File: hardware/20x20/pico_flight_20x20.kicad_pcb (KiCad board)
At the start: 2 copper layers, 28 x 28 mm, 39 parts, among them J1 USB_B_Micro, J4 ESC_AIKON32, U1 MCP1711T-33I_OT, U2 W25Q128JVS, U3 RP2040, U4 MPU-9250, Y1 SMD-3225_4P__12MHZ_20PF_10PPM

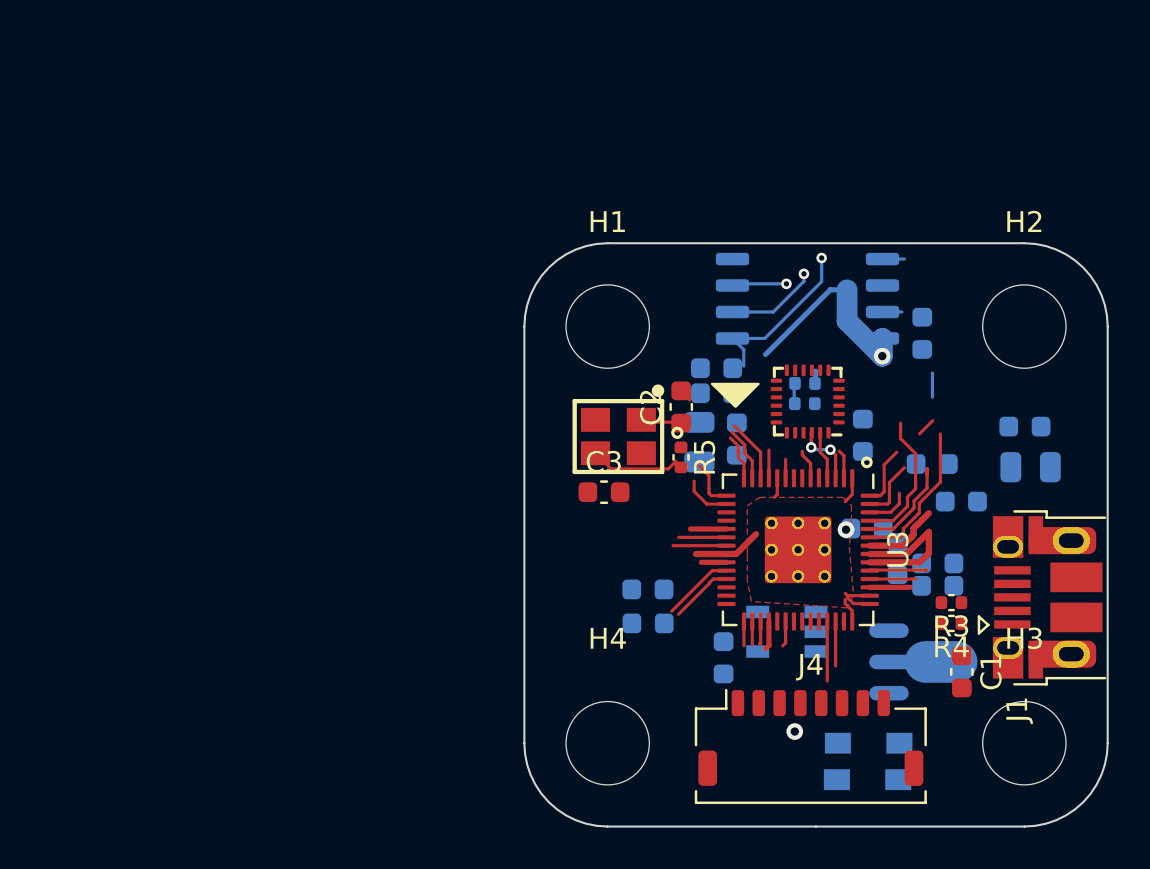
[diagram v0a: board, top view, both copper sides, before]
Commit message: Add implot, test mahi-gui, progress on pcb
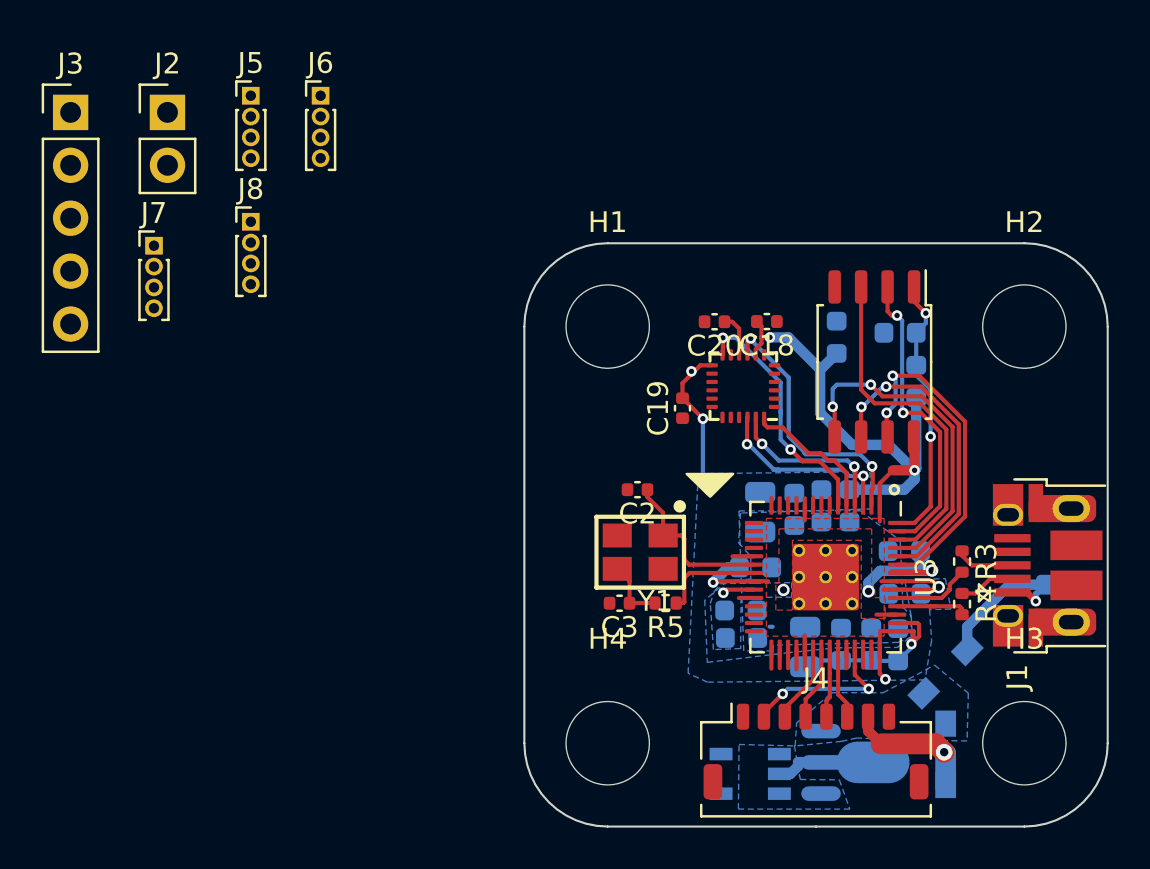
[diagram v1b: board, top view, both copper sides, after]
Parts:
- added J2: Conn_01x02, Connector_PinHeader_2.54mm:PinHeader_1x02_P2.54mm_Vertical, F.Cu at (-21.1, -10.3)
- added J3: DEBUG, Connector_PinHeader_2.54mm:PinHeader_1x05_P2.54mm_Vertical, F.Cu at (-25.8, -10.3)
- added J5: UART1, Connector_PinHeader_1.00mm:PinHeader_1x04_P1.00mm_Vertical, F.Cu at (-17.1, -11.1)
- added J6: UART2, Connector_PinHeader_1.00mm:PinHeader_1x04_P1.00mm_Vertical, F.Cu at (-13.8, -11.1)
- added J7: CAM, Connector_PinHeader_1.00mm:PinHeader_1x04_P1.00mm_Vertical, F.Cu at (-21.8, -3.88)
- added J8: VTX, Connector_PinHeader_1.00mm:PinHeader_1x04_P1.00mm_Vertical, F.Cu at (-17.1, -5.03)
- C1: moved to B.Cu
- C18, C19, C20: footprint Capacitor_SMD:C_0603_1608Metric -> Capacitor_SMD:C_0402_1005Metric; moved to F.Cu
- C2, C3: footprint Capacitor_SMD:C_0603_1608Metric -> Capacitor_SMD:C_0402_1005Metric
- R1, R2: footprint Capacitor_SMD:C_0402_1005Metric -> Capacitor_SMD:C_0603_1608Metric
- R3, R4, R5: footprint Capacitor_SMD:C_0402_1005Metric -> Resistor_SMD:R_0402_1005Metric
- U2: moved to F.Cu
- moved C4 13.8 mm to (9.48, 15.4), turned to 90 degrees
- moved C11 12.8 mm to (12.7, 15.2), turned to 90 degrees
- moved C7 12.4 mm to (6.42, 14.9)
- moved C19 8.86 mm to (3.59, 3.92), turned to 90 degrees
- moved U1 7.04 mm to (6.84, 21.5)
- moved R5 7.03 mm to (2.78, 13.3), turned to 180 degrees
- moved C13 6.83 mm to (7.09, 11.6), turned to 0 degrees
- moved C9 6.37 mm to (14.3, 12.8), turned to 180 degrees
- moved C1 6.36 mm to (21.8, 12.4), turned to 0 degrees
- moved C16 6.29 mm to (11.6, 8.61), turned to 270 degrees
- moved VR2 5.82 mm to (10.2, 20.9)
- moved R1 5.70 mm to (14.0, 0.30), turned to 180 degrees
- moved C15 5.68 mm to (11.2, 15.2)
- moved Y1 5.65 mm to (1.56, 10.8)
- moved C3 5.38 mm to (0.57, 13.3), turned to 180 degrees
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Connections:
- net VIDEO_IN renamed Net-(U3-Pad41)
- net VIDEO_OUT_SIG renamed Net-(U3-Pad18)
- net VIDEO_OUT_SYNC renamed Net-(U3-Pad17)
- U3 pad 34: Net-(U3-Pad34) -> ESC_MOTOR_4
- U3 pad 35: Net-(U3-Pad35) -> ESC_MOTOR_3
- U3 pad 36: Net-(U3-Pad36) -> ESC_MOTOR_2
- U3 pad 37: Net-(U3-Pad37) -> ESC_MOTOR_1
- U3 pad 39: Net-(U3-Pad39) -> ESC_CURRENT
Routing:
- net +3V3: track 28.4 -> 58.9 mm, vias 2 -> 8
- net /QSPI_SD2: track 4.72 -> 16.6 mm, vias 1 -> 0
- net IMU_DATA_RDY: track 1.47 -> 13.0 mm, vias 0 -> 2
- net IMU_SPI_MISO: track 1.39 -> 12.9 mm, vias 0 -> 2
- net /QSPI_SCLK: track 5.01 -> 15.1 mm, vias 0 -> 2
- net /QSPI_SD0: track 7.60 -> 16.6 mm, vias 0 -> 2
- net Net-(C1-Pad1): track 0.00 -> 7.99 mm, vias 0 -> 1
- net ESC_CURRENT: track 0.00 -> 7.90 mm, vias 0 -> 2
- net /QSPI_SD1: track 7.34 -> 14.8 mm, vias 1 -> 2
- net /QSPI_SD3: track 9.07 -> 16.3 mm, vias 0 -> 2
- net IMU_SPI_MOSI: track 0.42 -> 6.81 mm
- net VBAT: track 0.00 -> 6.37 mm, vias 0 -> 1
- net IMU_SPI_CS: track 3.15 -> 9.26 mm
- net IMU_SPI_SCLK: track 2.32 -> 8.13 mm, vias 0 -> 2
- net +1V1: track 6.83 -> 11.1 mm, vias 0 -> 4
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- added copper zone on B.Cu, net +1V1
- added copper zone on F.Cu, net +1V1
- added copper zone on B.Cu, net +3V3
- added copper zone on B.Cu, net +5V
- added copper zone on B.Cu, net GND
- added copper zone on B.Cu, net VBUS

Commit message: 45 degree layout
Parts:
- moved C3 6.21 mm to (4.58, 18.0), turned to 225 degrees
- moved C2 5.73 mm to (1.34, 13.6), turned to 225 degrees
- moved Y1 5.15 mm to (3.55, 15.6), turned to 225 degrees
- moved R4 4.69 mm to (16.2, 8.70), turned to 225 degrees
- moved R5 4.62 mm to (6.14, 16.4), turned to 225 degrees
- moved C1 4.10 mm to (21.9, 8.29)
- moved J1 4.10 mm to (22.4, 7.36)
- moved C10 4.04 mm to (14.9, 11.3), turned to 135 degrees
- moved C18 3.76 mm to (5.24, 2.66)
- moved C19 3.76 mm to (1.19, 6.82)
- moved C20 3.76 mm to (2.73, 2.67)
- moved U4 3.76 mm to (4.11, 5.76)
- moved C8 3.68 mm to (11.9, 7.95), turned to 225 degrees
- moved C9 3.56 mm to (13.4, 9.38), turned to 225 degrees
- moved R3 3.55 mm to (15.6, 8.04), turned to 225 degrees
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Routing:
- net +3V3: track 58.9 -> 29.1 mm, vias 8 -> 5
- net /QSPI_SD2: track 16.6 -> 0.00 mm
- net /QSPI_SD0: track 16.6 -> 1.49 mm, vias 2 -> 1
- net /QSPI_SD3: track 16.3 -> 2.01 mm
- net /QSPI_SCLK: track 15.1 -> 1.59 mm
- net IMU_SPI_MISO: track 12.9 -> 1.76 mm, vias 2 -> 1
- net IMU_DATA_RDY: track 13.0 -> 2.12 mm, vias 2 -> 0
- net /QSPI_SS: track 13.2 -> 4.91 mm, vias 2 -> 1
- net IMU_SPI_SCLK: track 8.13 -> 0.00 mm, vias 2 -> 0
- net ESC_CURRENT: track 7.90 -> 0.00 mm, vias 2 -> 0
- net /QSPI_SD1: track 14.8 -> 7.68 mm
- net IMU_SPI_MOSI: track 6.81 -> 0.00 mm
- net /XIN: track 8.05 -> 2.51 mm
- net IMU_SPI_CS: track 9.26 -> 3.82 mm
- net /XOUT: track 5.00 -> 0.00 mm
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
